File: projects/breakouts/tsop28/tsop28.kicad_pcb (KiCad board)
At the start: 2 copper layers, 38.1 x 12.7 mm, 3 parts, among them K1 TSSOP-28, K2 DIP, K3 DIP

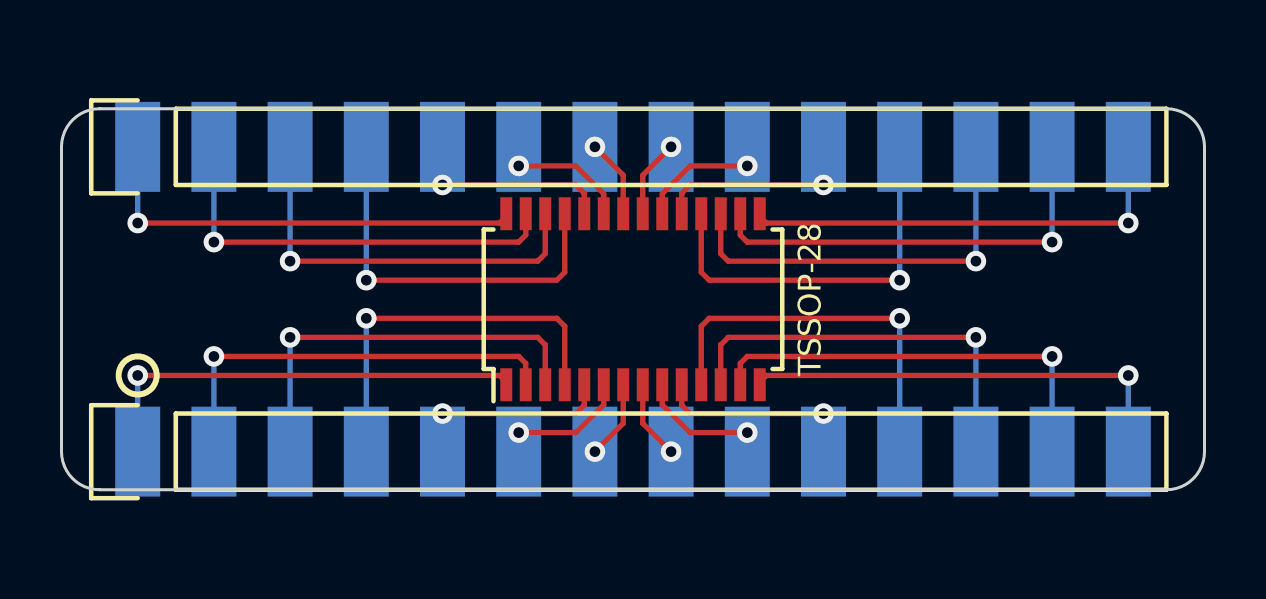
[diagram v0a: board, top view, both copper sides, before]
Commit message: Fixed some last minute bugs on drum master board, and added a TVS diode across 3.3v / 5v rails.
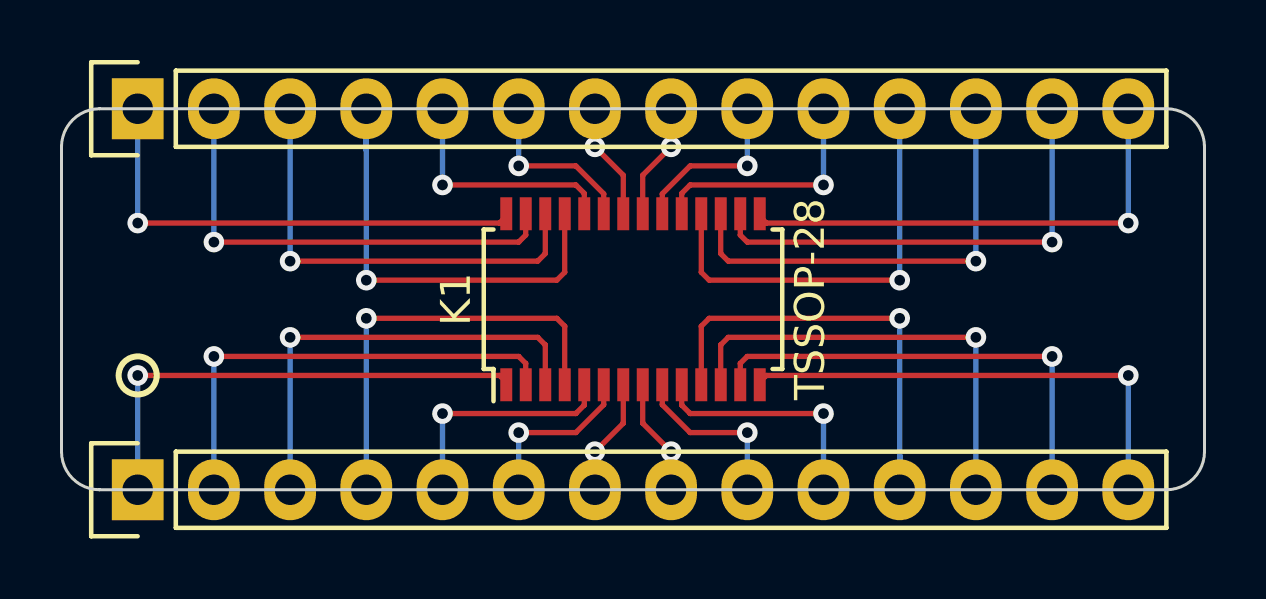
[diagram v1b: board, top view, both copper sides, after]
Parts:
- moved K2 1.27 mm to (68.6, 44.5)
- moved K3 1.27 mm to (68.6, 31.8)
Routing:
- net Net-(K1-Pad25): track 13.4 -> 17.2 mm
- net Net-(K1-Pad11): track 13.4 -> 16.7 mm
- net Net-(K1-Pad9): track 4.52 -> 5.79 mm
- net Net-(K1-Pad8): track 2.62 -> 3.89 mm
- net Net-(K1-Pad7): track 2.62 -> 3.89 mm
- net Net-(K1-Pad6): track 4.52 -> 5.79 mm
- net Net-(K1-Pad5): track 6.79 -> 8.06 mm
- net Net-(K1-Pad4): track 13.1 -> 14.4 mm
- net Net-(K1-Pad3): track 13.7 -> 15.0 mm
- net Net-(K1-Pad28): track 15.0 -> 16.3 mm
- net Net-(K1-Pad27): track 14.4 -> 15.6 mm
- net Net-(K1-Pad26): track 13.7 -> 15.0 mm
- net Net-(K1-Pad24): track 6.79 -> 8.06 mm
- net Net-(K1-Pad23): track 4.52 -> 5.79 mm
- net Net-(K1-Pad22): track 2.62 -> 3.89 mm
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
